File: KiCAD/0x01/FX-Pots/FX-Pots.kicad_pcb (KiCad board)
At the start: 2 copper layers, 100 x 100 mm, 57 parts, among them J1 IN, J2 OUT, SW1 SW_Push_LED, SW2 SW_Push_LED, SW3 SW_Push_LED, SW4 SW_Push_LED, SW5 SW_Push_LED, SW6 SW_Push_LED, SW7 SW_Push_LED, SW8 SW_Push_LED, U1 ADS7830, U2 ADS7830

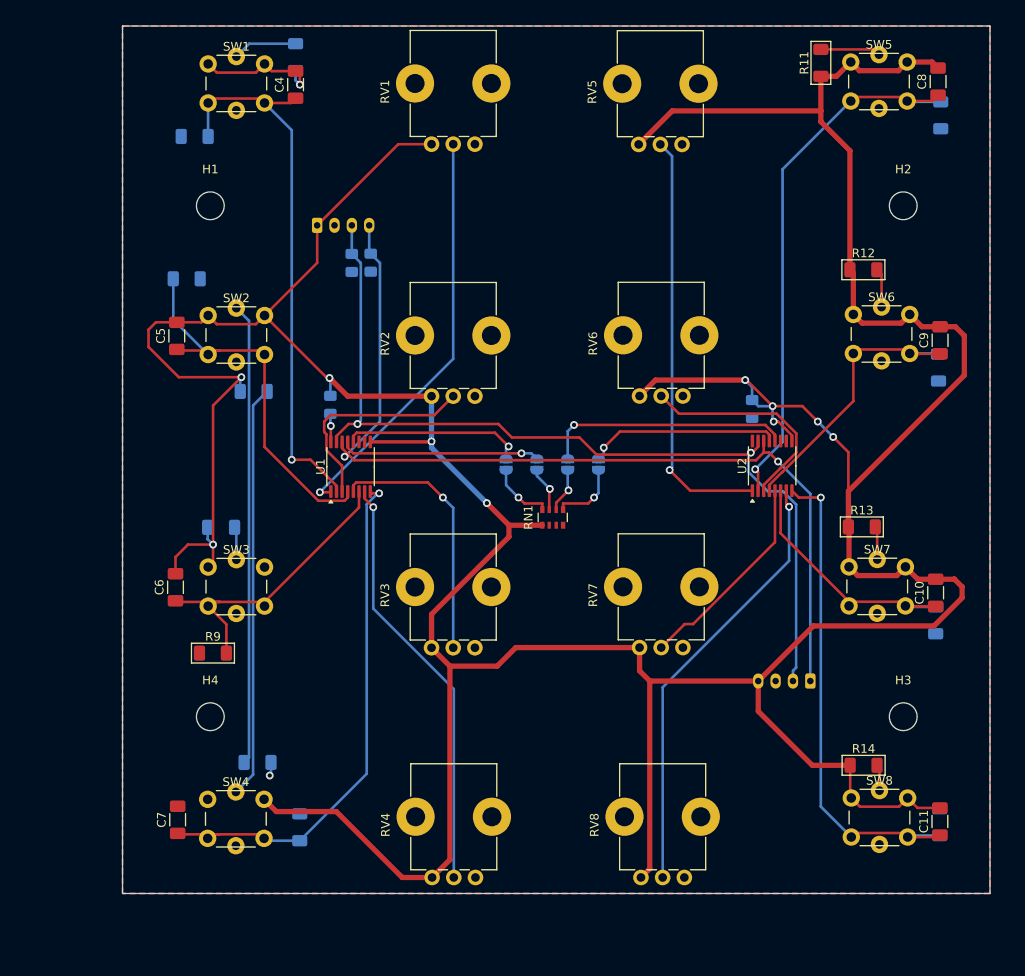
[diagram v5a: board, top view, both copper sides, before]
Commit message: pots refactor
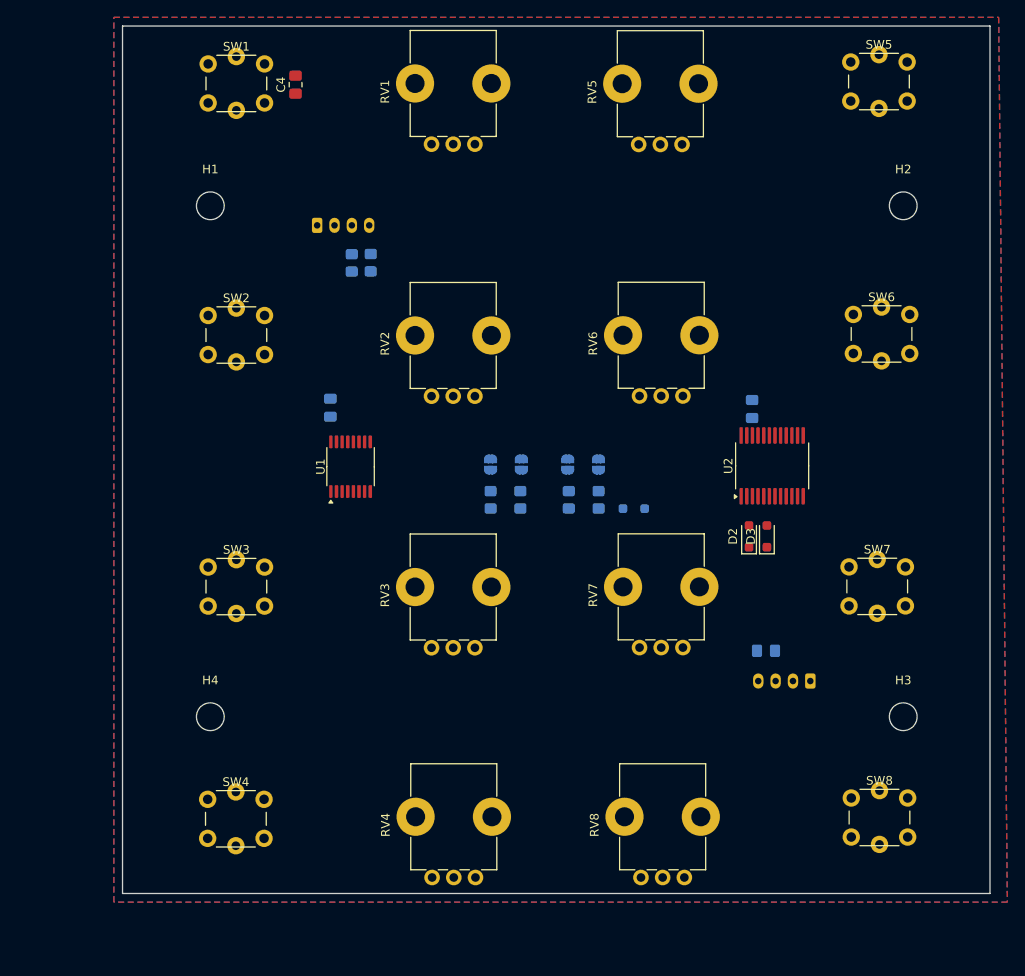
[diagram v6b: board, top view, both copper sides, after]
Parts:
- removed C10, C11, C5, C6, C7, C8, C9: 1uF, Capacitor_SMD:C_1206_3216Metric_Pad1.33x1.80mm_HandSolder
- removed R10, R15, R16, R17, R18, R7, R8, R9: 10K, PCM_Resistor_SMD_AKL:R_1206_3216Metric_Pad1.30x1.75mm_HandSolder
- removed R11, R12, R13, R14: 220, PCM_Resistor_SMD_AKL:R_1206_3216Metric_Pad1.30x1.75mm_HandSolder
- removed RN1: R_Pack04_10K, Resistor_SMD:R_Array_Convex_4x0603
- added C3: 10uF, Capacitor_SMD:C_0805_2012Metric_Pad1.18x1.45mm_HandSolder, B.Cu at (154.2, 112.0)
- added D1: 1N4148, Diode_SMD:D_SOD-323_HandSoldering, B.Cu at (138.9, 95.6)
- added D2: 1N4148, Diode_SMD:D_SOD-323_HandSoldering, F.Cu at (152.2, 98.8)
- added D3: 1N4148, Diode_SMD:D_SOD-323_HandSoldering, F.Cu at (154.3, 98.8)
- C4: value 1uF -> 10uF; footprint Capacitor_SMD:C_1206_3216Metric_Pad1.33x1.80mm_HandSolder -> Capacitor_SMD:C_0805_2012Metric_Pad1.18x1.45mm_HandSolder
- R1, R2: footprint Capacitor_SMD:C_0805_2012Metric_Pad1.18x1.45mm_HandSolder -> Resistor_SMD:R_0805_2012Metric_Pad1.20x1.40mm_HandSolder
- R3, R4: value 220 -> 47K; footprint PCM_Resistor_SMD_AKL:R_1206_3216Metric_Pad1.30x1.75mm_HandSolder -> Resistor_SMD:R_0805_2012Metric_Pad1.20x1.40mm_HandSolder
- R5, R6: value 220 -> 10K; footprint PCM_Resistor_SMD_AKL:R_1206_3216Metric_Pad1.30x1.75mm_HandSolder -> Resistor_SMD:R_0805_2012Metric_Pad1.20x1.40mm_HandSolder
- RV1, RV2, RV3, RV4, RV5, RV6, RV7, RV8: footprint led-switch:Potentiometer_Bourns_PTV09A-1_Single_Vertical -> Potentiometer_THT:Potentiometer_Bourns_PTV09A-1_Single_Vertical
- U2: value ADS7830 -> HT16K33 24SOP; footprint Package_SO:TSSOP-16_4.4x5mm_P0.65mm -> Package_SO:SSOP-24_5.3x8.2mm_P0.65mm
- moved R3 60.0 mm to (131.4, 94.6), turned to -90 degrees
- moved R4 49.6 mm to (134.9, 94.6), turned to -90 degrees
- moved R6 33.2 mm to (125.9, 94.6), turned to -90 degrees
- moved R5 31.2 mm to (122.4, 94.6), turned to -90 degrees
- moved JP1 1.79 mm to (122.4, 90.6)
- moved JP2 1.79 mm to (126.0, 90.6)
- moved C1 0.33 mm to (104.0, 84.0)
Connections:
- C4 pad 1: /FXSW1 -> +5V
- JP3 pad 1: /A3 -> /A0_H
- JP4 pad 1: /A4 -> /A1_H
- R3 pad 1: GND -> Net-(JP3-B)
- R3 pad 2: Net-(SW1-K) -> Net-(D1-K)
- R4 pad 1: GND -> Net-(JP4-B)
- R4 pad 2: Net-(SW2-K) -> Net-(D1-K)
- R5 pad 1: GND -> Net-(JP1-B)
- R5 pad 2: Net-(SW3-K) -> GND
- R6 pad 1: GND -> Net-(JP2-B)
- R6 pad 2: Net-(SW4-K) -> GND
- SW1 pad 1: GND -> /R3
- SW1 pad 2: /FXSW1 -> Net-(D2-K)
- SW1 pad 3: Net-(SW1-K) -> /COM0
- SW1 pad 4: /FX-LED-1 -> /A1_H
- SW2 pad 1: GND -> /R4
- SW2 pad 2: /FXSW2 -> Net-(D2-K)
- SW2 pad 3: Net-(SW2-K) -> /COM0
- SW2 pad 4: /FX-LED-2 -> /A0_H
- SW3 pad 1: GND -> /R5
- SW3 pad 2: /FXSW3 -> Net-(D2-K)
- SW3 pad 3: Net-(SW3-K) -> /COM0
- SW3 pad 4: /FX-LED-3 -> /R4
- SW4 pad 1: GND -> /R6
- SW4 pad 2: /FXSW4 -> Net-(D2-K)
- SW4 pad 3: Net-(SW4-K) -> /COM0
- SW4 pad 4: /FX-LED-4 -> /R5
- SW5 pad 1: GND -> /R7
- SW5 pad 2: /FXSW5 -> Net-(D3-K)
- SW5 pad 3: Net-(SW5-K) -> /COM1
- SW5 pad 4: /FX-LED-5 -> /R2
- SW6 pad 1: GND -> /R8
- SW6 pad 2: /FXSW6 -> Net-(D3-K)
- SW6 pad 3: Net-(SW6-K) -> /COM1
- SW6 pad 4: /FX-LED-6 -> /R3
- SW7 pad 1: GND -> /R9
- SW7 pad 2: /FXSW7 -> Net-(D3-K)
- SW7 pad 3: Net-(SW7-K) -> /COM1
- SW7 pad 4: /FX-LED-7 -> /R6
- SW8 pad 1: GND -> /R10
- SW8 pad 2: /FXSW8 -> Net-(D3-K)
- SW8 pad 3: Net-(SW8-K) -> /COM1
- SW8 pad 4: /FX-LED-8 -> /R7
- U1 pad 2: /FXSW1 -> /POT5
- U1 pad 4: /FXSW2 -> /POT6
- U1 pad 6: /FXSW3 -> /POT7
- U1 pad 8: /FXSW4 -> /POT8
- U2 pad 1: /POT5 -> GND
- U2 pad 11: unconnected-(U2-COM-Pad11) -> /R10
- U2 pad 12: /A3 -> /R9
- U2 pad 13: /A4 -> /R8
- U2 pad 14: /SCL -> /R7
- U2 pad 15: /SDA -> /R6
- U2 pad 16: +5V -> /R5
- U2 pad 2: /FXSW5 -> /COM0
- U2 pad 3: /POT6 -> /COM1
- U2 pad 4: /FXSW6 -> /COM2
- U2 pad 5: /POT7 -> unconnected-(U2-COM3/KS2-Pad5)
- U2 pad 6: /FXSW7 -> unconnected-(U2-COM4-Pad6)
- U2 pad 7: /POT8 -> unconnected-(U2-COM5-Pad7)
- U2 pad 8: /FXSW8 -> unconnected-(U2-COM6-Pad8)
- U2 pad 9: GND -> unconnected-(U2-COM7-Pad9)
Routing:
- net GND: track 529.7 -> 0.00 mm, vias 12 -> 0
- net /SCL: track 109.9 -> 0.00 mm, vias 2 -> 0
- net /SDA: track 105.7 -> 0.00 mm, vias 2 -> 0
- net /FXSW5: track 64.3 -> 0.00 mm, vias 1 -> 0
- net /FXSW1: track 64.1 -> 0.00 mm, vias 1 -> 0
- net /FXSW4: track 61.0 -> 0.00 mm, vias 1 -> 0
- net /FXSW8: track 58.7 -> 0.00 mm, vias 1 -> 0
- net Net-(SW2-K): track 53.2 -> 0.00 mm
- net /POT8: track 50.8 -> 0.00 mm, vias 1 -> 0
- net /POT4: track 48.7 -> 0.00 mm, vias 1 -> 0
- net /POT5: track 48.7 -> 0.00 mm, vias 1 -> 0
- net /POT1: track 47.8 -> 0.00 mm, vias 1 -> 0
- net Net-(SW4-K): track 47.7 -> 0.00 mm
- net /FXSW2: track 45.9 -> 0.00 mm
- net /FXSW3: track 35.9 -> 0.00 mm
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- removed copper zone on F.Cu, net +5V

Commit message: finished fx-pots & encoders-lcd
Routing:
- net Net-(D2-K): track 0.00 -> 175.0 mm
- net /COM0: track 0.00 -> 154.5 mm, vias 0 -> 1
- net GND: track 0.00 -> 132.0 mm, vias 0 -> 8
- net Net-(D3-K): track 0.00 -> 129.5 mm
- net /R5: track 0.00 -> 115.4 mm
- net /R4: track 0.00 -> 112.2 mm, vias 0 -> 1
- net /R6: track 0.00 -> 111.9 mm, vias 0 -> 1
- net /SCL: track 0.00 -> 108.6 mm, vias 0 -> 2
- net /SDA: track 0.00 -> 108.2 mm, vias 0 -> 2
- net /R3: track 0.00 -> 107.9 mm
- net /COM1: track 0.00 -> 107.4 mm
- net /R7: track 0.00 -> 105.5 mm, vias 0 -> 1
- net /A1_H: track 0.00 -> 85.9 mm, vias 0 -> 2
- net /POT8: track 0.00 -> 75.6 mm, vias 0 -> 1
- net /A0_H: track 0.00 -> 73.8 mm, vias 0 -> 1
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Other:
- board text added: "GND 5V SDA SCL"

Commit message: step models
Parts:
- RV1, RV2, RV3, RV4, RV5, RV6, RV7, RV8: footprint Potentiometer_THT:Potentiometer_Bourns_PTV09A-1_Single_Vertical -> led-sw:Potentiometer_Bourns_PTV09A-1_Single_Vertical
